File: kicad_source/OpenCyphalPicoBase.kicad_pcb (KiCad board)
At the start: 2 copper layers, 69 x 37 mm, 63 parts, among them CN1 RASPBERRYPI_PICO, CN10 1x04, CN11 CONN_01X03, CN12 CONN_01X03, CN2 SM04B-SRSS-TB, CN3 SM04B-SRSS-TB, CN4 GH_SM04B-GHS-TB, CN5 GH_SM04B-GHS-TB, CN6 691322310002, CN7 CONN_02X03, CN8 01X08, CN9 1x04, SW1 SPST, U3 24LC64, U8 MCP2515, U9 SN65HVD232, Y1 16MHz

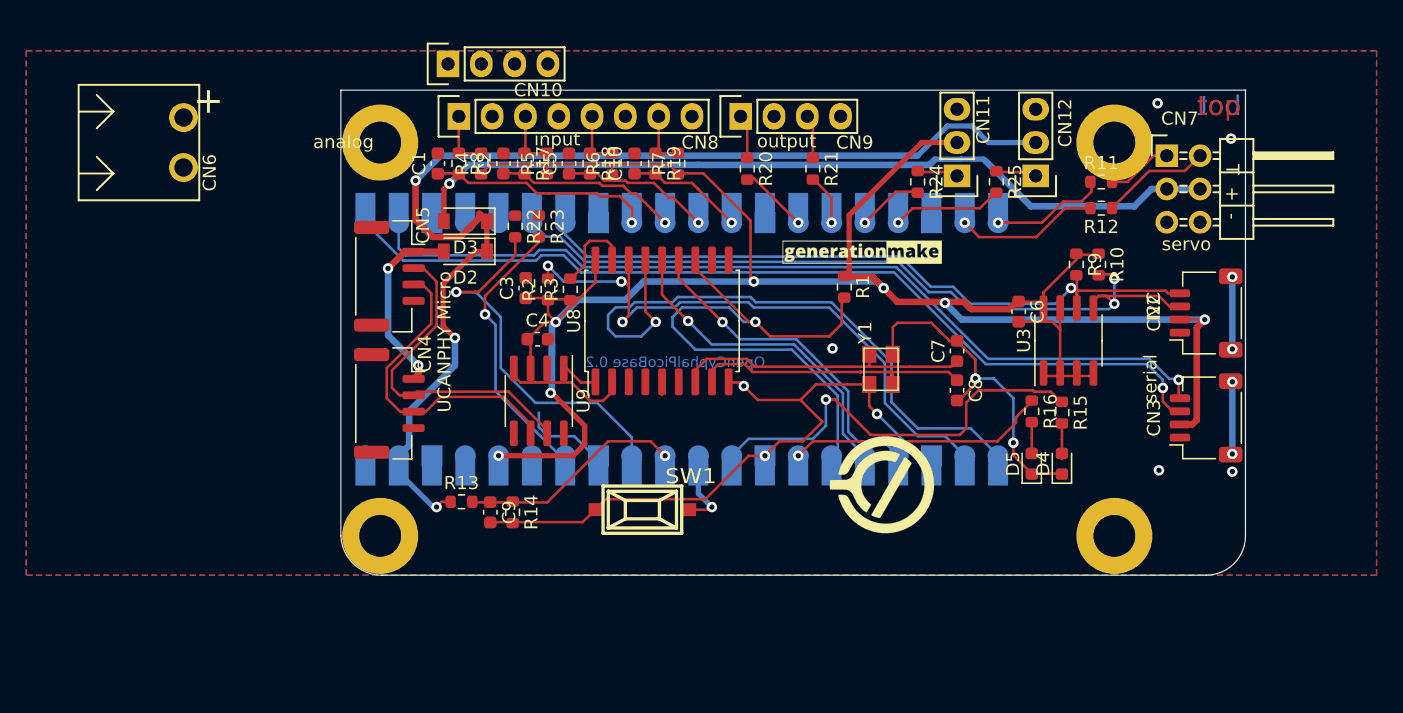
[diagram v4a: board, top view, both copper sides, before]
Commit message: changed some connectors
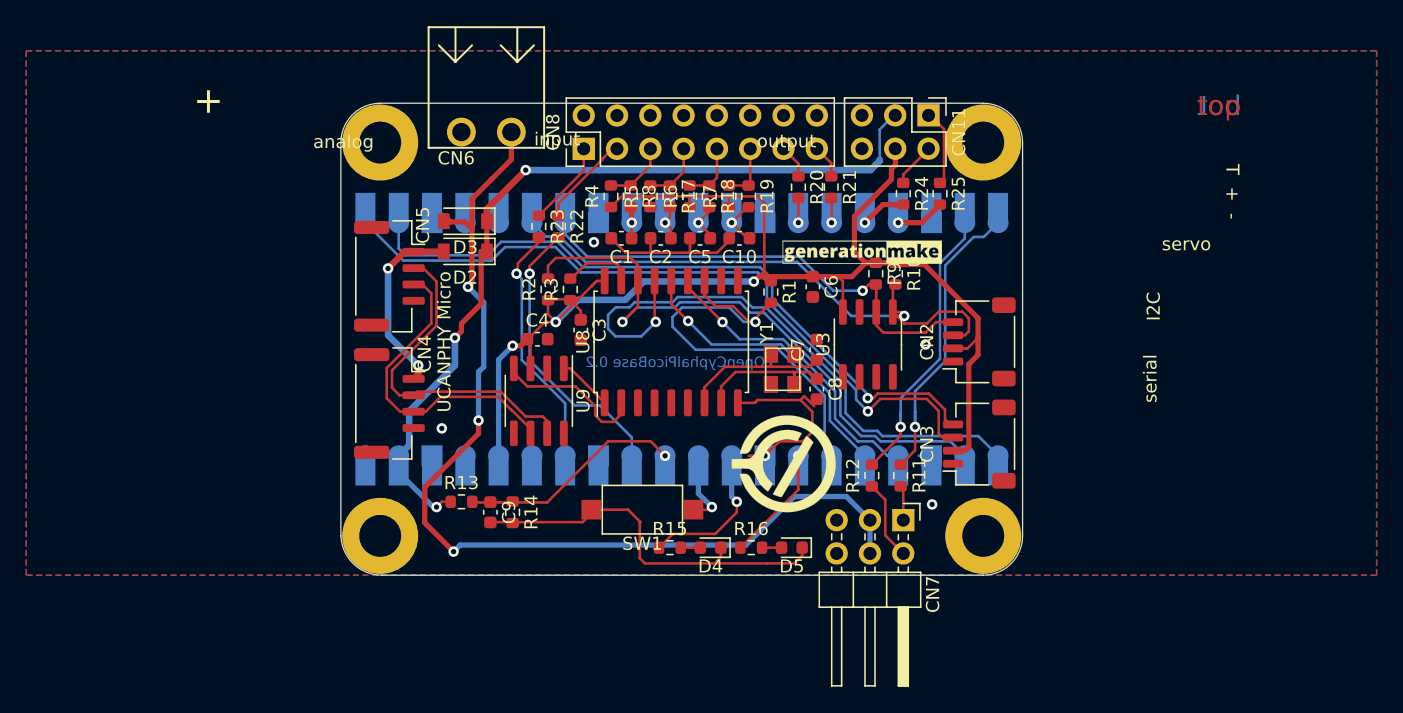
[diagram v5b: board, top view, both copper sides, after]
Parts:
- removed CN10, CN9: 1x04, pin_headers:Pin_Header_Straight_1x04
- removed CN12: CONN_01X03, pin_headers:Pin_Header_Straight_1x03
- CN11: value CONN_01X03 -> CONN_02X03; footprint pin_headers:Pin_Header_Straight_1x03 -> Connector_PinHeader_2.54mm:PinHeader_2x03_P2.54mm_Vertical
- CN7: footprint pin_headers:Pin_Header_Angled_2x03 -> Connector_PinHeader_2.54mm:PinHeader_2x03_P2.54mm_Horizontal
- CN8: value 01X08 -> Conn_02x08_Odd_Even; footprint pin_headers:Pin_Header_Straight_1x08 -> Connector_PinHeader_2.54mm:PinHeader_2x08_P2.54mm_Vertical
- SW1: footprint mechanical-switches:WE_434121050816 -> Button_Switch_SMD:SW_SPST_CK_RS282G05A3
- moved CN7 34.3 mm to (106.9, 105.8), turned to -90 degrees
- moved R15 31.6 mm to (89.1, 107.9), turned to 0 degrees
- moved D4 27.6 mm to (92.2, 107.9), turned to 180 degrees
- moved R11 27.1 mm to (106.7, 102.4), turned to -90 degrees
- moved R12 26.9 mm to (104.5, 102.4), turned to 90 degrees
- moved R16 23.8 mm to (95.3, 107.9), turned to 0 degrees
- moved CN6 23.1 mm to (75.1, 76.2), turned to 180 degrees
- moved D5 19.4 mm to (98.4, 107.9), turned to 180 degrees
- moved CN2 17.4 mm to (112.7, 92.2)
- moved CN3 17.4 mm to (112.7, 100.0)
- moved C6 15.8 mm to (100.0, 88.0)
- moved R10 15.5 mm to (106.3, 87.0)
- moved R9 15.3 mm to (104.8, 87.0)
- moved U3 15.3 mm to (104.2, 92.4)
- moved C1 15.1 mm to (85.4, 84.3), turned to 180 degrees
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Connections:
- CN11 pad 1: /RESERVED0_R -> /NEOPIXEL_R
- CN11 pad 2: +3V3 -> /RESERVED0_R
- CN11 pad 3: GND -> +BATT
- CN8 pad 1: /INPUT0_R -> /ANALOG_INPUT1_R
- CN8 pad 3: /INPUT1_R -> /ANALOG_INPUT0_R
- CN8 pad 5: /INPUT2_R -> /INPUT0_R
- CN8 pad 7: /INPUT3_R -> /INPUT1_R
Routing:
- net +3V3: track 187.5 -> 113.6 mm, vias 8 -> 3
- net +BATT: track 89.1 -> 64.0 mm
- net GND: track 84.0 -> 59.4 mm, vias 10 -> 5
- net /LED3: track 33.5 -> 11.5 mm
- net /I2C_SCL: track 55.3 -> 37.4 mm
- net /I2C_SDA: track 60.8 -> 44.9 mm, vias 2 -> 1
- net /SER_RX: track 68.7 -> 53.7 mm
- net /INPUT0: track 18.3 -> 3.76 mm
- net /SERVO1: track 10.1 -> 24.1 mm
- net /SER_TX: track 70.7 -> 56.8 mm
- net /V_IN: track 63.1 -> 76.3 mm, vias 1 -> 3
- net /MCP2515/MCP2515_OSC1: track 21.8 -> 10.2 mm
- net /INPUT1: track 15.2 -> 4.05 mm
- net /MCP2515/MCP2515_OSC2: track 22.7 -> 11.6 mm
- net /SERVO0: track 12.3 -> 23.4 mm
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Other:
- board size 69 x 37 mm -> 52 x 36 mm

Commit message: added NeoPixel connector, updated layout
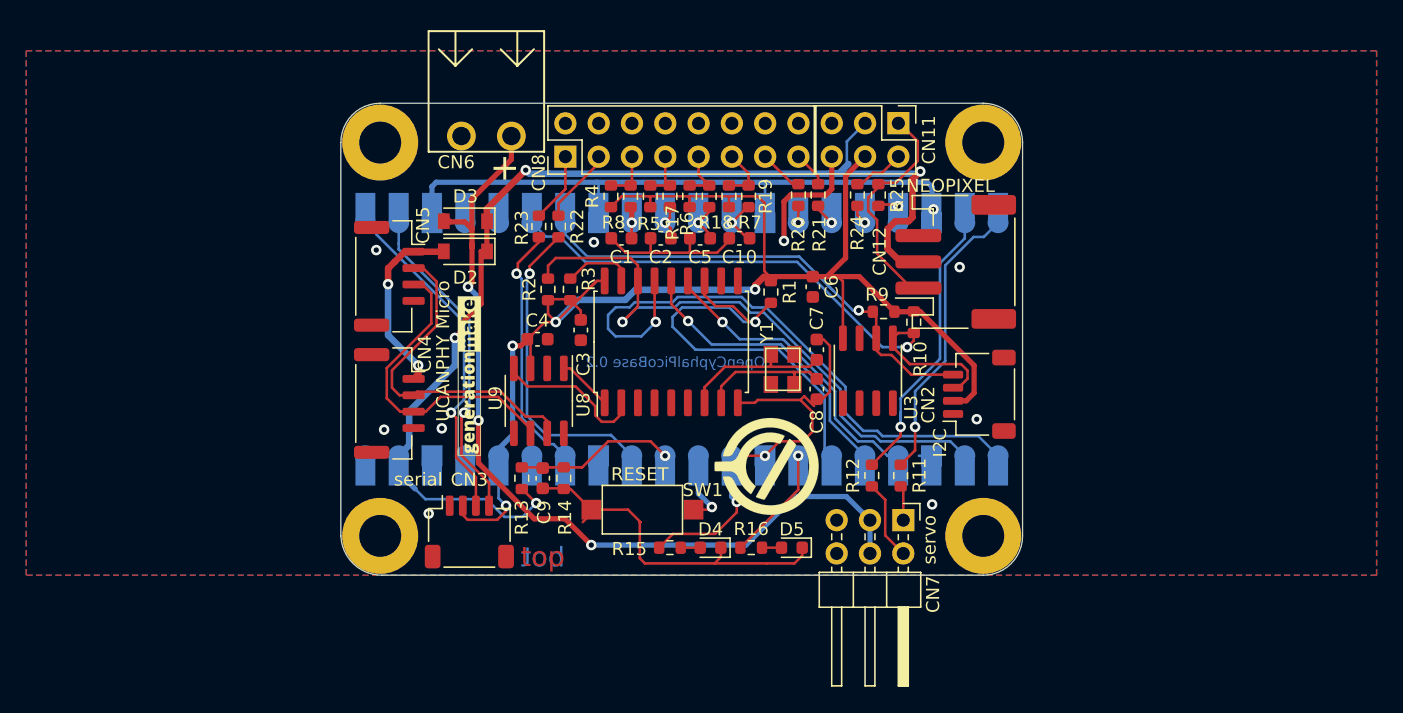
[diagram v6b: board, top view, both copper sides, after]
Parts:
- added CN12: Conn_01x03, Connector_JST:JST_PH_S3B-PH-SM4-TB_1x03-1MP_P2.00mm_Horizontal, F.Cu at (110.9, 86.1)
- moved CN3 39.5 mm to (73.8, 106.7), turned to 0 degrees
- moved L1 28.2 mm to (76.4, 94.8), turned to 90 degrees
- moved L2 6.00 mm to (85.6, 108.4)
- moved R13 4.94 mm to (77.8, 102.6), turned to 90 degrees
- moved C9 4.77 mm to (79.4, 102.6)
- moved R25 4.70 mm to (105.0, 81.0)
- moved R14 4.69 mm to (81.0, 102.6)
- moved CN2 4.00 mm to (112.7, 96.2)
- moved R10 3.96 mm to (107.7, 90.7)
- moved R24 3.50 mm to (103.4, 81.0)
- moved R9 2.96 mm to (105.4, 89.9), turned to 180 degrees
- moved CN11 2.38 mm to (106.5, 75.5)
- moved U3 2.00 mm to (104.2, 94.4)
- moved CN8 1.52 mm to (81.1, 78.1)
- moved L3 1.32 mm to (96.5, 101.7)
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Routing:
- net GND: track 59.4 -> 117.3 mm, vias 5 -> 11
- net /SER_TX: track 56.8 -> 27.2 mm
- net /SER_RX: track 53.7 -> 26.7 mm
- net +BATT: track 64.0 -> 87.5 mm, vias 3 -> 4
- net /NEOPIXEL_R: track 5.88 -> 17.4 mm
- net /V_IN: track 76.3 -> 67.1 mm
- net /+BATT_MEAS: track 18.5 -> 13.5 mm
- net /NEOPIXEL: track 5.03 -> 2.83 mm
- net /ANALOG_INPUT0: track 23.2 -> 25.1 mm
- net /RESERVED0: track 4.77 -> 2.89 mm
- net /ANALOG_INPUT0_R: track 7.15 -> 5.77 mm
- net +3V3: track 113.6 -> 112.2 mm, vias 3 -> 4
- net /ANALOG_INPUT1_R: track 6.52 -> 5.34 mm
- net /INPUT0_R: track 4.92 -> 3.74 mm
- net /I2C_SDA: track 44.9 -> 46.0 mm
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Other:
- board text added: "NEOPIXEL"
- board text added: "RESET"
- board text removed: "RESERVED1"
- board text removed: "T + -"
- board text removed: "analog"
- board text removed: "input"
- board text removed: "output"

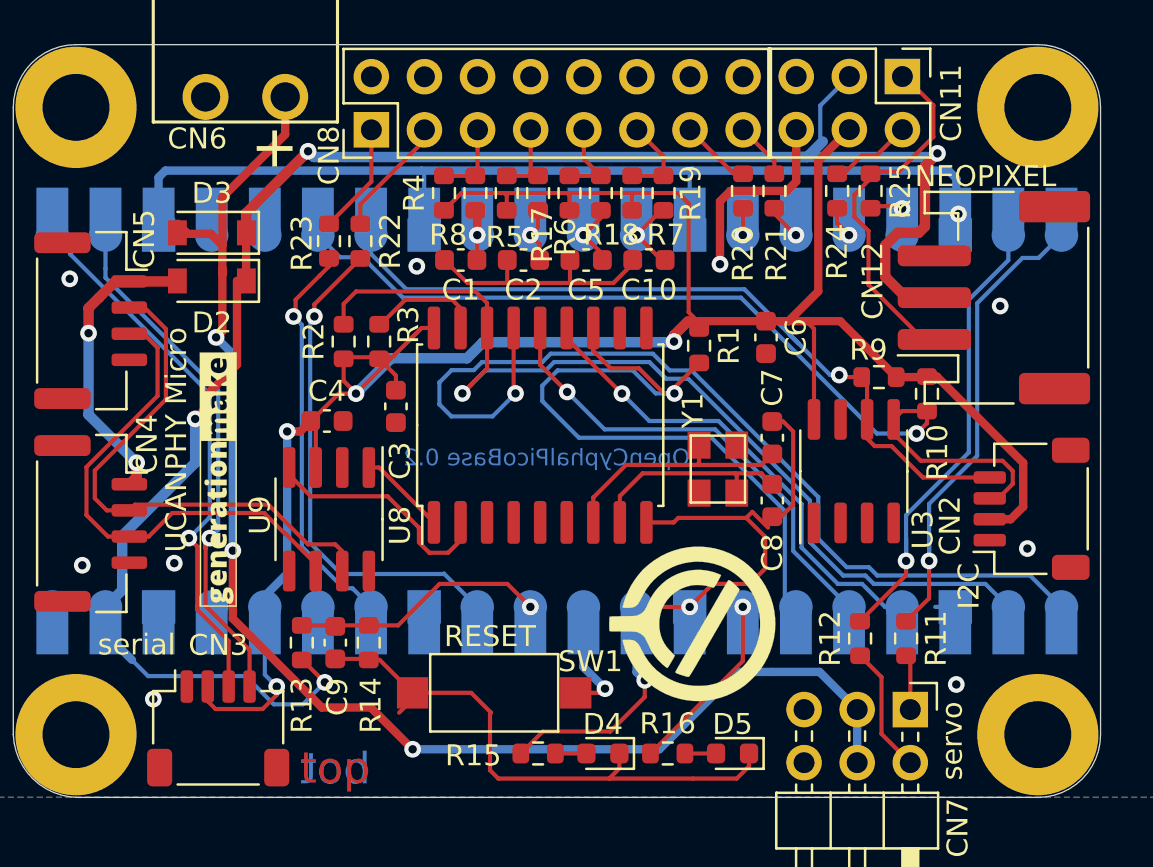
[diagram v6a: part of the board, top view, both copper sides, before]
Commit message: fixed some drc errors
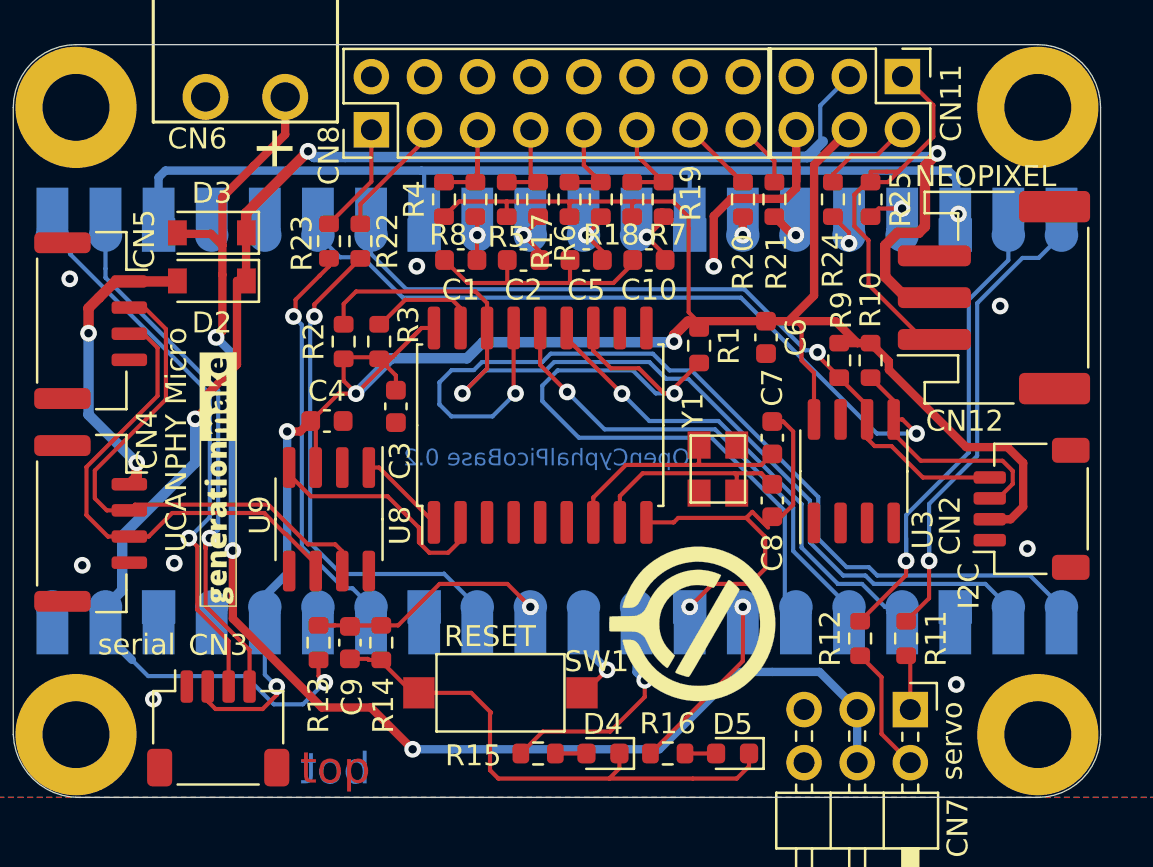
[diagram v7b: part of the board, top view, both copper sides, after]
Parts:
- moved R10 3.14 mm to (105.0, 89.1)
- moved R9 2.06 mm to (103.5, 89.1), turned to -90 degrees
- moved R13 0.80 mm to (78.6, 102.6)
- moved C9 0.70 mm to (80.1, 102.6)
- moved R14 0.60 mm to (81.6, 102.6)
- moved R24 0.45 mm to (103.2, 81.4)
- moved R20 0.40 mm to (98.9, 81.4)
- moved R21 0.40 mm to (100.4, 81.4)
- moved R25 0.40 mm to (105.0, 81.4)
- moved R17 0.30 mm to (89.1, 81.4)
- moved R18 0.30 mm to (92.1, 81.4)
- moved R19 0.30 mm to (95.1, 81.4)
- moved R4 0.30 mm to (84.6, 81.4)
- moved R5 0.30 mm to (87.6, 81.4)
- moved R6 0.30 mm to (90.6, 81.4)
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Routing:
- net /NEOPIXEL_R: track 17.4 -> 19.1 mm
- net GND: track 117.3 -> 115.9 mm
- net /INPUT0_R: track 3.74 -> 5.07 mm
- net /I2C_SCL: track 38.4 -> 37.2 mm
- net /RESET: track 6.12 -> 5.13 mm
- net /MCP2515/CANL: track 25.2 -> 24.2 mm
- net /+BATT_MEAS: track 13.5 -> 12.7 mm
- net /I2C_SDA: track 46.0 -> 46.8 mm
- net /OUTPUT0: track 2.95 -> 2.16 mm
- net MCP2515_CS: track 47.9 -> 47.2 mm
- net /RESERVED0_R: track 3.96 -> 4.58 mm
- net +3V3: track 112.2 -> 112.9 mm

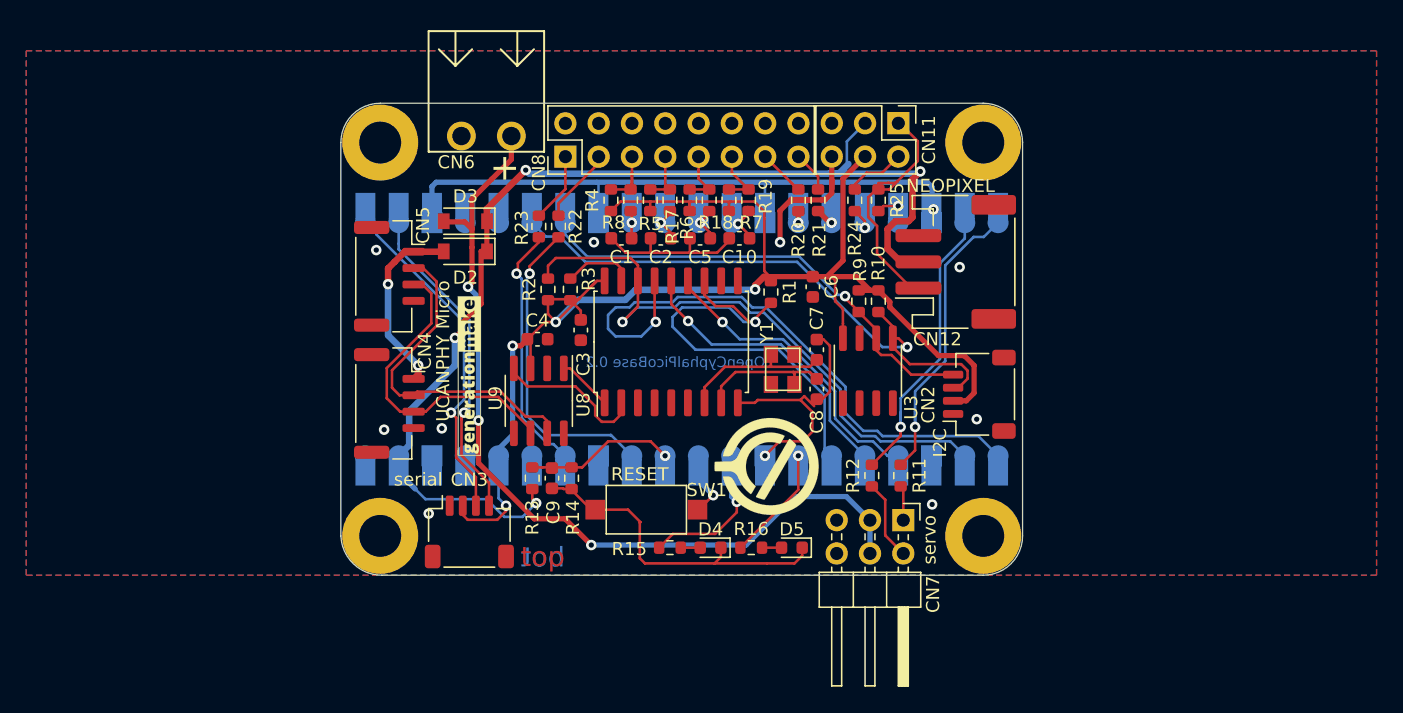
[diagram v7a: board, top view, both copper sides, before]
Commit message: switched servos to +BATT to power them from CAN bus
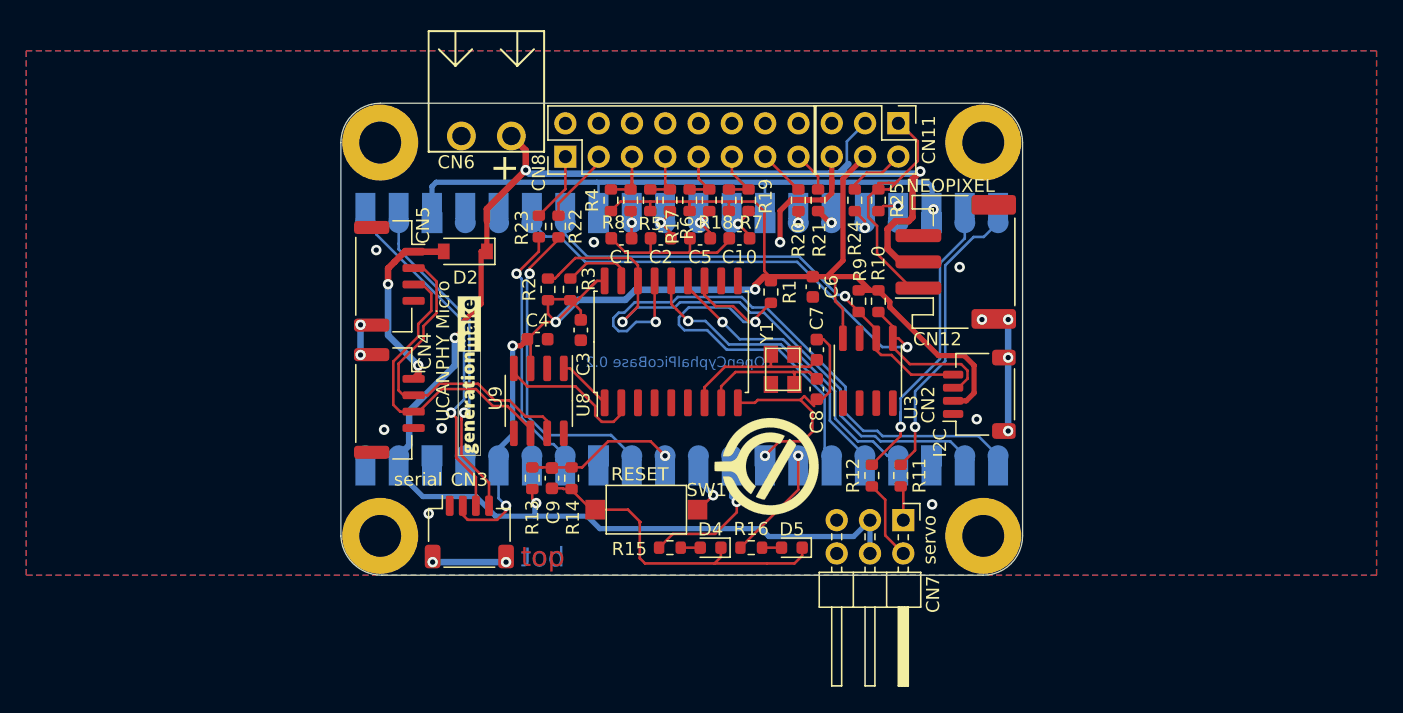
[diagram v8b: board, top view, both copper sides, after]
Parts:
- removed D3: MBR0530T1G, Diode_SMD:D_SOD-123
- moved L2 4.72 mm to (89.6, 110.9)
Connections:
- CN6 pad 1: /V_IN -> +BATT
- CN7 pad 3: /V_IN -> +BATT
- CN7 pad 4: /V_IN -> +BATT
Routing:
- net /V_IN: track 66.7 -> 0.00 mm, vias 3 -> 0
- net +BATT: track 87.1 -> 119.9 mm
- net (no net): track 0.00 -> 18.4 mm, vias 0 -> 8
- net MISO: track 46.3 -> 44.9 mm
- net MCP2515_INT: track 35.4 -> 34.4 mm
- net MCP2515_CS: track 47.2 -> 46.6 mm
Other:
- board text added: "V_IN | GND"
- board text added: "find data and documentation at https://github.com/generationmake/OpenCyphalPicoBase"
- board text removed: "GND | V_IN"
